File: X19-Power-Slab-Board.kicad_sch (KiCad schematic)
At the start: 33 parts, among them J2 796636-6, J3 Conn_01x02_Pin, J4 Conn_01x04_Pin, J5 Conn_01x04_Pin, Q1 TSM340N06CP_ROG, U2 MIC5504-3.3YM5-TR, U3 INA237AIDGSR, U4 TMP1075NDRLR, U6 TCAN1044AVDRQ1

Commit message: Nick's changes
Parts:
- added C9: 1uF, SOT-23-5_MC_MCH, symbol Device:C
- added R15: 4.7K, symbol Device:R_US
- added R3: 4.7k, symbol Device:R_US
- C5: value 0.1uF -> 1uF
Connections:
- net 3.3V: no longer U4.5 (V+)
- net 5.2V: now also C9.1
- net GND: now also U4.4 (A0), C9.2
- net SCL: now also U3.5 (SCL), U4.1 (SCL)
- net SDA: now also U3.4 (SDA), U4.6 (SDA)
- net at U3.3 (ALERT): now also R15.2
- net at U4.3 (ALERT): now also R3.2
- new net +3.3V: R3.1, U4.5 (V+)
- new net +3V3: R15.1
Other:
- sheet STM32 MCU and Power Bricks renamed MCU
- added sheet Power (power.kicad_sch)
- note added: "I2C Address: 0x40"
- note added: "I2C Address: 0xF4628"
- note added: "I2C Pull ups"
- note added: "Place Near STM"
- note added: "TODO: change power to the arrow symbol"
- note removed: "I2C"
- note removed: "double click to access schematic"
- moved on the sheet: C5, TP4

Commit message: Updated MCU
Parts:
- removed C5, C9: 1uF, SOT-23-5_MC_MCH, symbol Device:C
- removed R10, R9: 4.7k, symbol Device:R_US
- removed U2: MIC5504-3.3YM5-TR, SOT-23-5_MC_MCH, symbol 2026-09-18_23-52-43:MIC5504-3.3YM5-TR
- added J5, J6: Conn_01x05, symbol Connector_Generic:Conn_01x05
- renumbered D6 to D2, D2 to D3, D5 to D4, D4 to D5, J4 to J1, J3 to J2, J5 to J3, J2 to J4, R8 to R2, R2 to R3, R7 to R4, R4 to R5, R5 to R6, R15 to R7, R3 to R8, R6 to R9, TP2 to TP1, TP1 to TP2, U6 to U1, U3 to U2, U4 to U3
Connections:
- net +3.3V: now also J1.4 (Pin_4), R4.2, TP5.1, U1.5 (VIO), U2.6 (VS)
- net 48V_RAW: no longer R9.1, U2.10 (IN+)
- net CAN_H: now also J5.1 (Pin_1)
- net CAN_L: now also J6.1 (Pin_1)
- net GND: now also J5.2 (Pin_2), J6.4 (Pin_4)
- net at D3.2 (A): now also R3.1; no longer R3.2
- net at D1.2 (A): now also R1.1; no longer R1.2
- net at D4.2 (A): now also R4.1; no longer R4.2
- net at R5.2: now also R6.2; no longer R6.1
- net at D5.2 (A): now also R6.1; no longer R6.2
- net 12V renamed +12V
- net +12V: now also R3.2, J6.5 (Pin_5); no longer R3.1
- removed net 3.3V: J1.4 (Pin_4), R4.1, TP5.1, U1.5 (VIO), U2.6 (VS)
- net 48V renamed +48V
- net 5.2V renamed +5.2V
- net +5.2V: now also R1.2, J5.5 (Pin_5); no longer R1.1
- new net +48V_RAW: R9.1, U2.10 (IN+)
- new net CS_Pi: J5.4 (Pin_4)
- new net MISO: J6.3 (Pin_3)
- new net MOSI: J5.3 (Pin_3)
- new net SCLK: J6.2 (Pin_2)
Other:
- note added: "Board Output Connectors"
- note removed: "3.3V LDO"
- note removed: "I2C Pull ups"
- note removed: "Place Near STM"
- note removed: "TODO: change power to the arrow symbol"
- moved on the sheet: D1, D2, D3, D4, D5, J1, J2, J3, J4, Q1, R1, R2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

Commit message: fix 48V caps, and add MCU NC
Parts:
- C1, C2, C3: value 330uF -> 680uF
- C4: value 0.1uF -> 4.7uF
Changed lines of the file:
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@@
 			)
 		)
-		(property "Value" "330uF"
+		(property "Value" "680uF"
 			(at 68.58 38.9381 0)
 			(show_name no)
@@
 			)
 		)
-		(property "Value" "330uF"
+		(property "Value" "680uF"
 			(at 40.64 38.9381 0)
 			(show_name no)
@@
 			)
 		)
-		(property "Value" "330uF"
+		(property "Value" "680uF"
 			(at 54.61 38.9381 0)
 			(show_name no)
@@
 			)
 		)
-		(property "Value" "0.1uF"
+		(property "Value" "4.7uF"
 			(at 83.82 39.3699 0)
 			(show_name no)

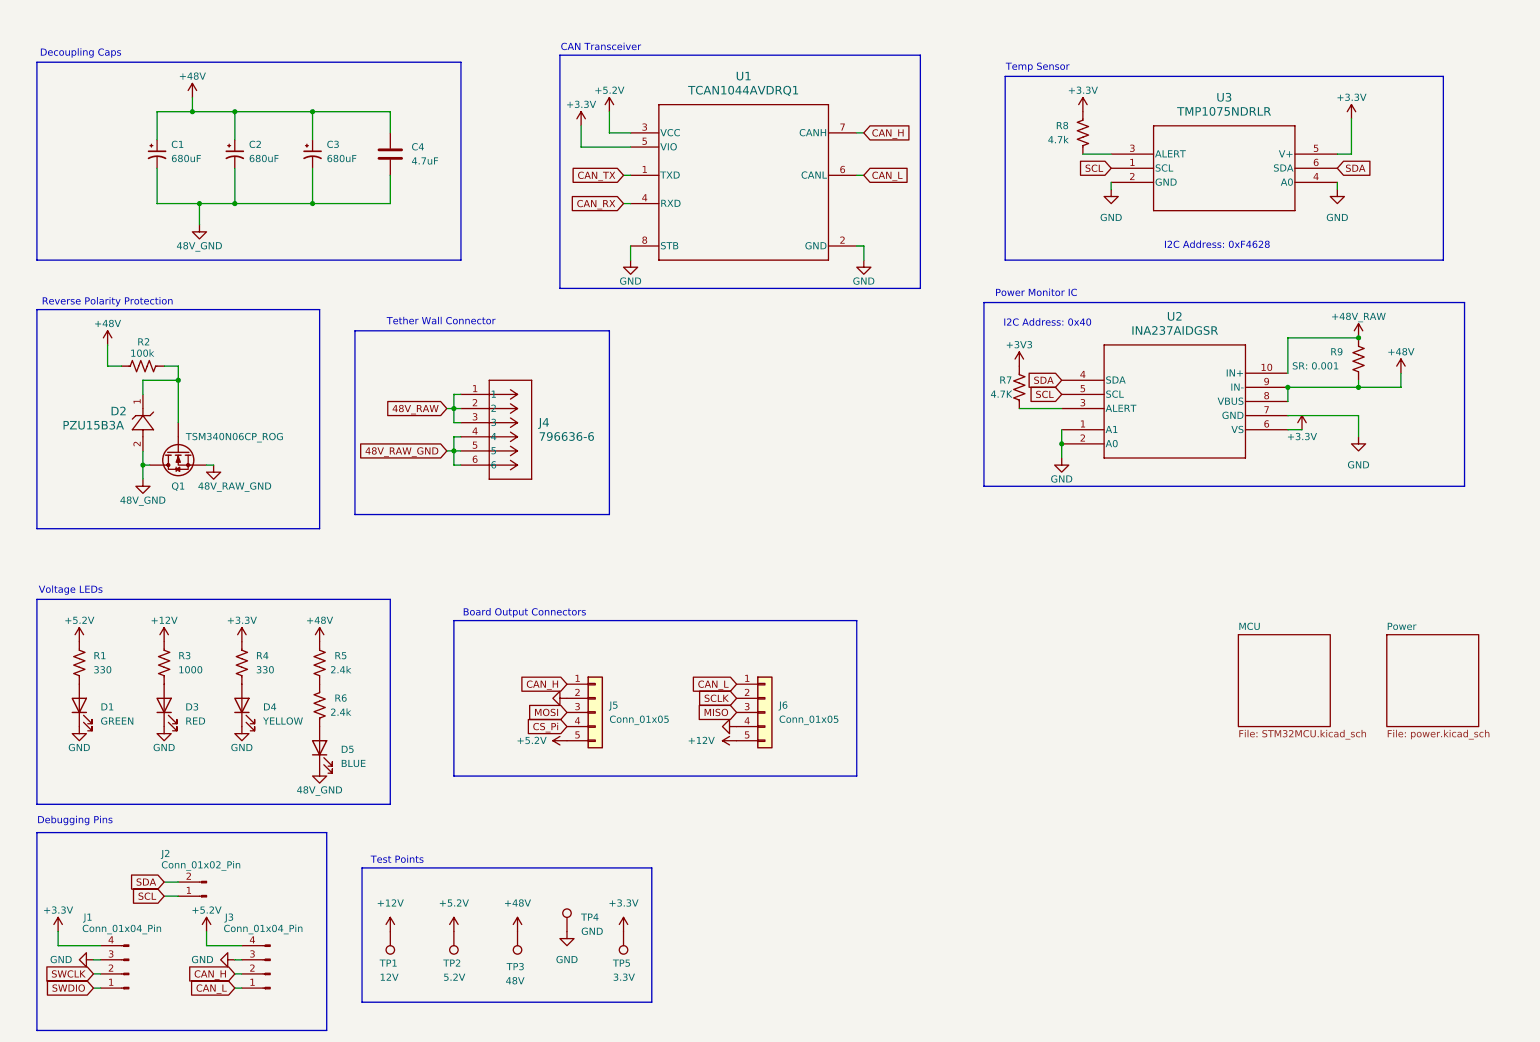
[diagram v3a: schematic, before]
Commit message: Add INA237 for 12V for each brick
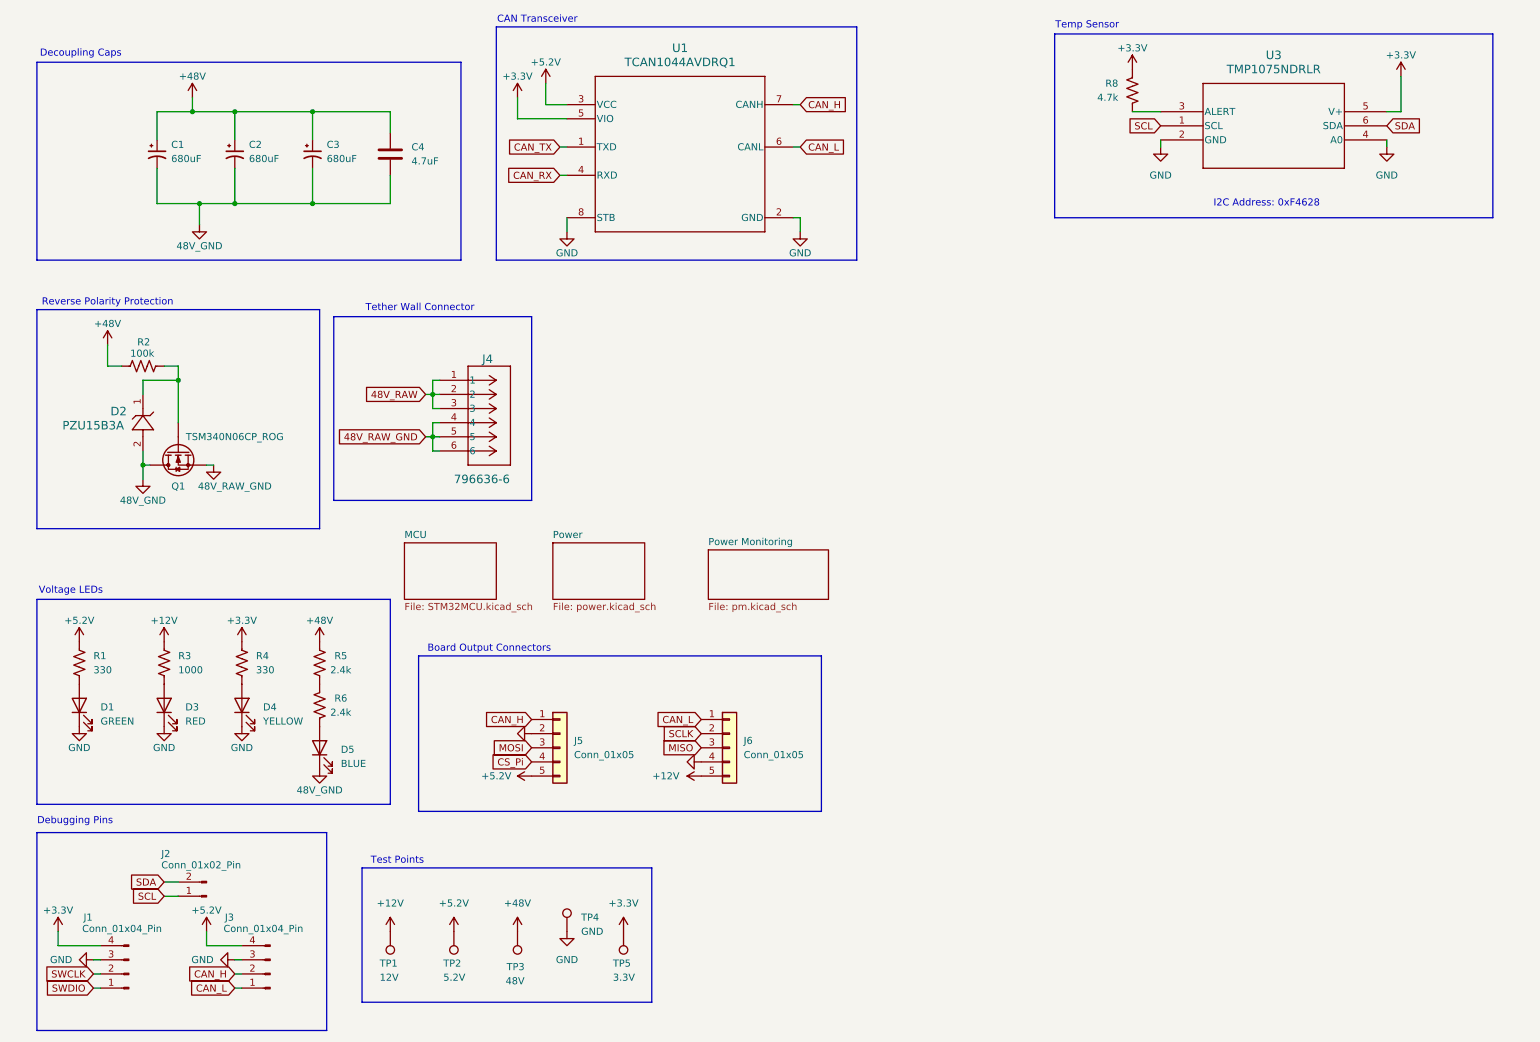
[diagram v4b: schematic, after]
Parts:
- removed R7: 4.7K, symbol Device:R_US
- removed R9: SR: 0.001, symbol Device:R_US
- removed U2: INA237AIDGSR, VSSOP_IDGSR_TEX, symbol 2026-09-19_00-01-31:INA237AIDGSR
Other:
- added sheet Power Monitoring (pm.kicad_sch)
- note removed: "I2C Address: 0x40"
- note removed: "Power Monitor IC"
- moved on the sheet: J4, J5, J6, R8, U1, U3

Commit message: Added decouping caps
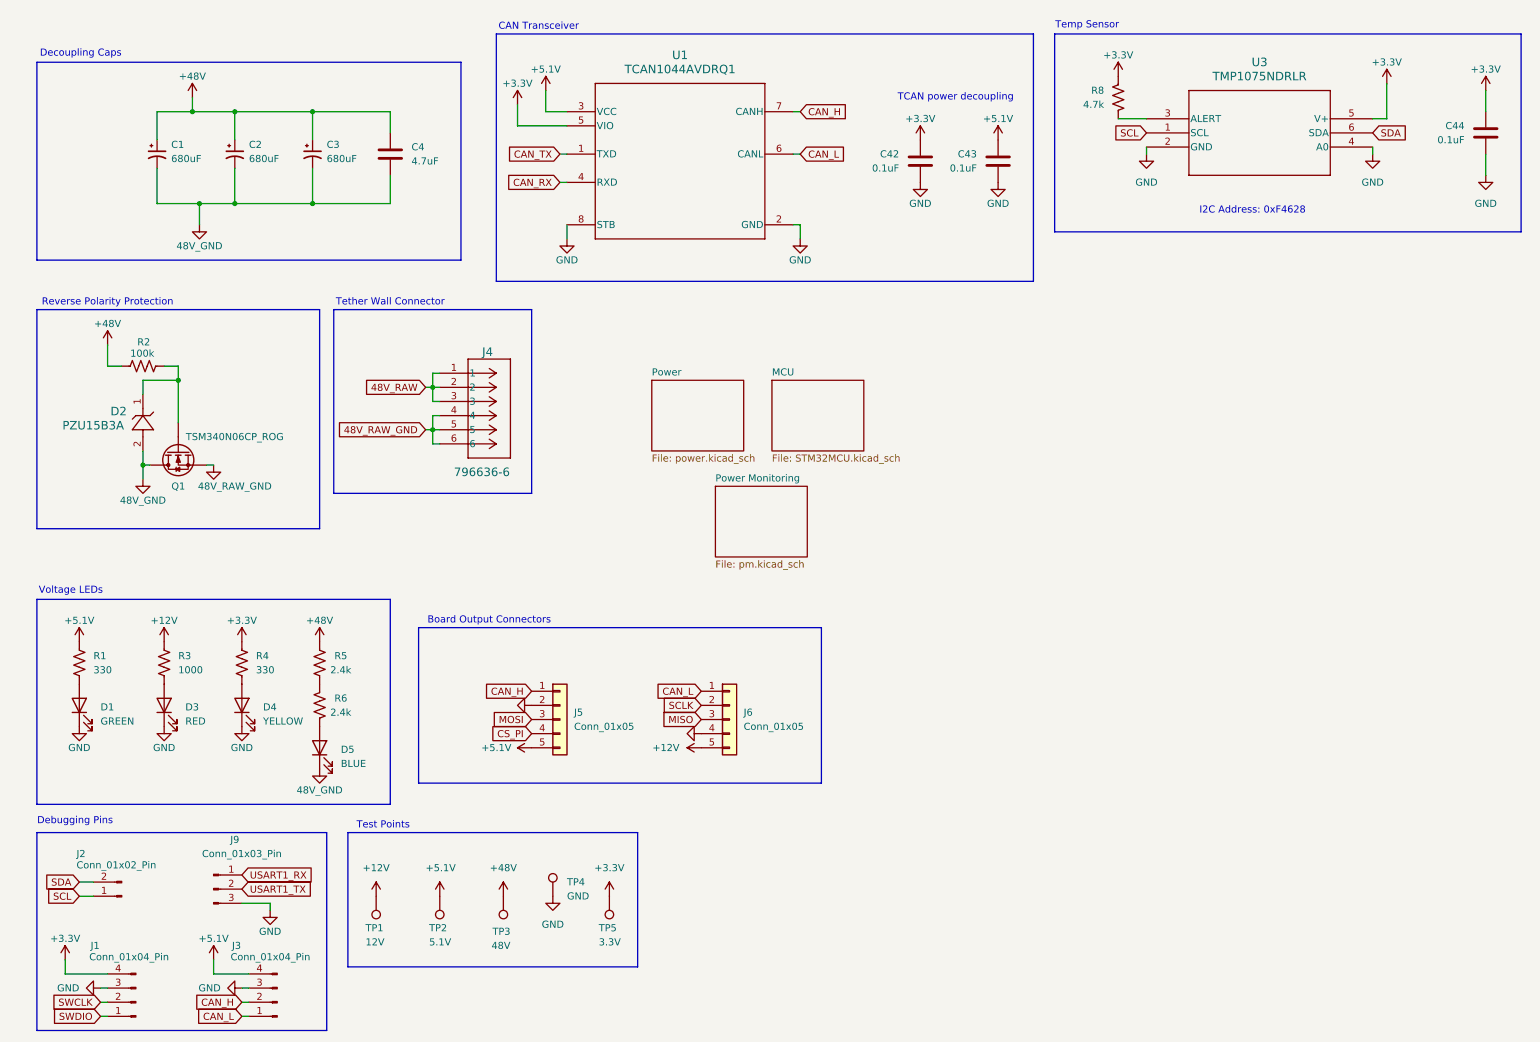
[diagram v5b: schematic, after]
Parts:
- added C42, C43, C44: 0.1uF, symbol Device:C
- added J9: Conn_01x03_Pin, symbol Connector:Conn_01x03_Pin
- TP2: value 5.2V -> 5.1V
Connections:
- net +3.3V: now also C42.1, C44.1
- net GND: now also C42.2, C43.2, C44.2, J9.3 (Pin_3)
- net +5.2V renamed +5.1V
- net +5.1V: now also C43.1
- net CS_Pi renamed CS_PI
- new net USART1_RX: J9.1 (Pin_1)
- new net USART1_TX: J9.2 (Pin_2)
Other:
- note added: "TCAN power decoupling"
- moved on the sheet: J1, J2, J3, J4, J5, J6, R8, TP1, TP2, TP3, TP4, TP5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

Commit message: Reverse polarity and power flow TBD, improved capacitance and labelling for nets
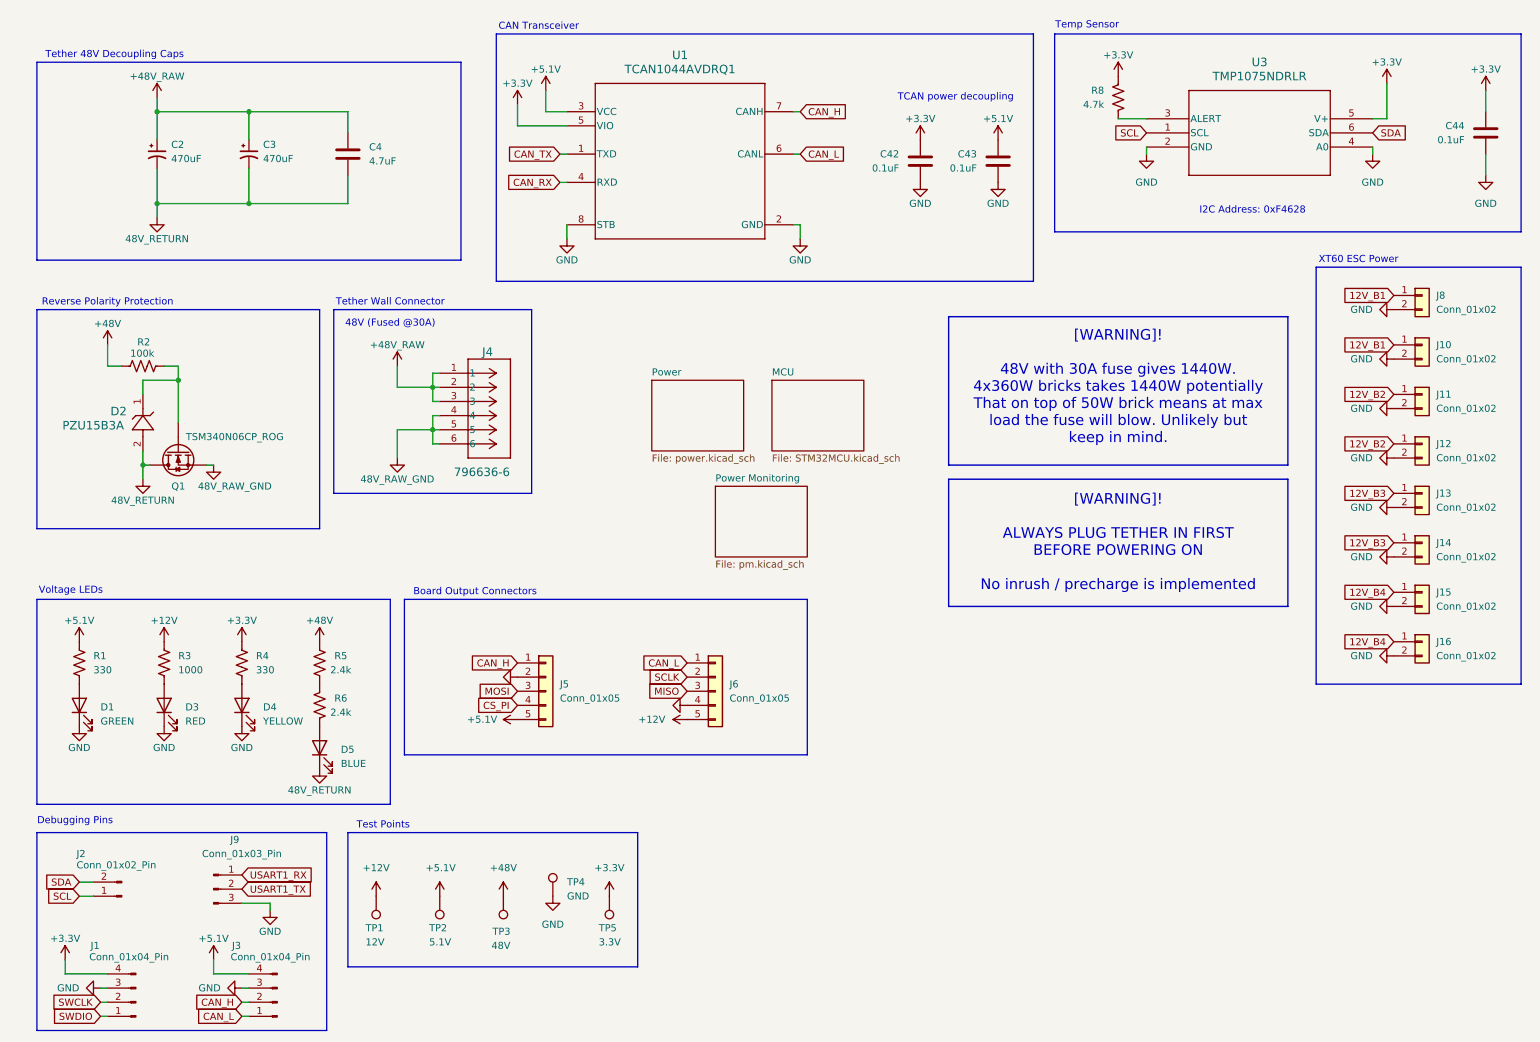
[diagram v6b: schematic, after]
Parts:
- removed C1: 680uF, symbol Device:C_Polarized_Small_US
- added J10, J11, J12, J13, J14, J15, J16, J8: Conn_01x02, symbol Connector_Generic:Conn_01x02
- C2, C3: value 680uF -> 470uF
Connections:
- net +48V: no longer C2.1, C3.1, C4.1
- net GND: now also J10.2 (Pin_2), J11.2 (Pin_2), J12.2 (Pin_2), J13.2 (Pin_2), J14.2 (Pin_2), J15.2 (Pin_2), J16.2 (Pin_2), J8.2 (Pin_2)
- net 48V_GND renamed 48V_RETURN
- net 48V_RAW renamed +48V_RAW
- net +48V_RAW: now also C2.1, C3.1, C4.1
- new net 12V_B1: J10.1 (Pin_1), J8.1 (Pin_1)
- new net 12V_B2: J11.1 (Pin_1), J12.1 (Pin_1)
- new net 12V_B3: J13.1 (Pin_1), J14.1 (Pin_1)
- new net 12V_B4: J15.1 (Pin_1), J16.1 (Pin_1)
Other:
- note added: "48V (Fused @30A)"
- note added: "Tether 48V Decoupling Caps"
- note added: "XT60 ESC Power"
- note added: "[WARNING]! 48V with 30A fuse gives 1440W. 4x360W bricks takes 1440W potentially That on top of 50W brick means at max load the fuse will blow. Unlikely but keep in mind."
- note added: "[WARNING]! ALWAYS PLUG TETHER IN FIRST BEFORE POWERING ON No inrush / precharge is implemented"
- note removed: "Decoupling Caps"
- moved on the sheet: C2, C3, C4, J5, J6
